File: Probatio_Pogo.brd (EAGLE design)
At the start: 21.5 x 8 mm, 5 parts

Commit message: Update Probatio_Pogo.brd
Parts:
- moved POGO1 2.00 mm to (4.00, 4.00)
- moved POGO2 2.00 mm to (7.00, 4.00)
- moved POGO3 2.00 mm to (10.0, 4.00)
- moved POGO4 2.00 mm to (13.0, 4.00)
- moved U$1 2.00 mm to (18.0, 4.00)
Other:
- board size 21.5 x 8 mm -> 23.5 x 8 mm
- board text added: "pogo-pcb v0.2.0"
- board text added: "probatio"
- board text removed: "Pogo-board v0.2.0"
- board text removed: "Probatio"
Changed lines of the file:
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@@
 <board>
 <plain>
-<wire x1="21.5" y1="1" x2="21.5" y2="7" width="0" layer="20"/>
+<wire x1="23.5" y1="1" x2="23.5" y2="7" width="0" layer="20"/>
 <wire x1="0" y1="7" x2="0" y2="1" width="0" layer="20"/>
-<wire x1="20.5" y1="8" x2="1" y2="8" width="0" layer="20"/>
-<text x="2.6" y="2.12" size="0.8128" layer="21" font="vector">1</text>
-<text x="5.4" y="2.09" size="0.8128" layer="21" font="vector">2</text>
-<text x="8.41" y="2.13" size="0.8128" layer="21" font="vector">3</text>
-<text x="11.51" y="2.14" size="0.8128" layer="21" font="vector">4</text>
-<text x="19.33" y="2.32" size="0.8128" layer="22" font="vector" rot="MR0">1</text>
-<text x="19.35" y="4.88" size="0.8128" layer="22" font="vector" rot="MR0">2</text>
-<text x="13.1" y="4.9" size="0.8128" layer="22" font="vector" rot="MR0">3</text>
-<text x="13.1" y="2.44" size="0.8128" layer="22" font="vector" rot="MR0">4</text>
-<wire x1="1" y1="0" x2="20.5" y2="0" width="0" layer="20"/>
+<wire x1="22.5" y1="8" x2="1" y2="8" width="0" layer="20"/>
+<text x="4.6" y="2.12" size="0.8128" layer="21" font="vector">1</text>
+<text x="7.4" y="2.09" size="0.8128" layer="21" font="vector">2</text>
+<text x="10.41" y="2.13" size="0.8128" layer="21" font="vector">3</text>
+<text x="13.51" y="2.14" size="0.8128" layer="21" font="vector">4</text>
+<text x="21.33" y="2.32" size="0.8128" layer="22" font="vector" rot="MR0">1</text>
+<text x="21.35" y="4.88" size="0.8128" layer="22" font="vector" rot="MR0">2</text>
+<text x="15.1" y="4.9" size="0.8128" layer="22" font="vector" rot="MR0">3</text>
+<text x="15.1" y="2.44" size="0.8128" layer="22" font="vector" rot="MR0">4</text>
+<wire x1="1" y1="0" x2="22.5" y2="0" width="0" layer="20"/>
 <wire x1="0" y1="7" x2="1" y2="8" width="0" layer="20" curve="-90"/>
 <wire x1="0" y1="1" x2="1" y2="0" width="0" layer="20" curve="90"/>
-<wire x1="20.5" y1="0" x2="21.5" y2="1" width="0" layer="20" curve="90"/>
-<wire x1="21.5" y1="7" x2="20.5" y2="8" width="0" layer="20" curve="90"/>
-<hole x="20.2" y="1.3" drill="2.2"/>
-<hole x="20.2" y="6.7" drill="2.2"/>
+<wire x1="22.5" y1="0" x2="23.5" y2="1" width="0" layer="20" curve="90"/>
+<wire x1="23.5" y1="7" x2="22.5" y2="8" width="0" layer="20" curve="90"/>
+<hole x="22.2" y="1.3" drill="2.2"/>
+<hole x="22.2" y="6.7" drill="2.2"/>
 <hole x="1.3" y="6.7" drill="2.2"/>
 <hole x="1.3" y="1.3" drill="2.2"/>
-<circle x="18.64" y="1.44" radius="0.183575" width="0.1524" layer="21"/>
-<circle x="2.97" y="4.96" radius="0.1627875" width="0.1524" layer="21"/>
-<text x="11.84" y="3.3" size="1.778" layer="22" font="vector" rot="MR0">Probatio</text>
-<text x="12" y="1" size="0.6096" layer="22" font="vector" rot="MR0">Pogo-board v0.2.0</text>
+<circle x="20.64" y="1.44" radius="0.183575" width="0.1524" layer="21"/>
+<circle x="4.97" y="4.96" radius="0.1627875" width="0.1524" layer="21"/>
+<text x="13.84" y="3.3" size="1.778" layer="22" font="vector" rot="MR0">probatio</text>
+<text x="14" y="1" size="0.6096" layer="22" font="vector" rot="MR0">pogo-pcb v0.2.0</text>
 </plain>
 <attributes>
@@
 </autorouter>
 <elements>
-<element name="POGO1" library="Batebit" package="POGO_PIN" value="POGO_PIN0900-0-15-20-76-14-11-0" x="2" y="4"/>
-<element name="POGO2" library="Batebit" package="POGO_PIN" value="POGO_PIN0900-0-15-20-76-14-11-0" x="5" y="4"/>
-<element name="POGO3" library="Batebit" package="POGO_PIN" value="POGO_PIN0900-0-15-20-76-14-11-0" x="8" y="4"/>
-<element name="POGO4" library="Batebit" package="POGO_PIN" value="POGO_PIN0900-0-15-20-76-14-11-0" x="11" y="4"/>
-<element name="U$1" library="Batebit" package="2X2" value="M02X22X2" x="16" y="4"/>
+<element name="POGO1" library="Batebit" package="POGO_PIN" value="POGO_PIN0900-0-15-20-76-14-11-0" x="4" y="4"/>
+<element name="POGO2" library="Batebit" package="POGO_PIN" value="POGO_PIN0900-0-15-20-76-14-11-0" x="7" y="4"/>
+<element name="POGO3" library="Batebit" package="POGO_PIN" value="POGO_PIN0900-0-15-20-76-14-11-0" x="10" y="4"/>
+<element name="POGO4" library="Batebit" package="POGO_PIN" value="POGO_PIN0900-0-15-20-76-14-11-0" x="13" y="4"/>
+<element name="U$1" library="Batebit" package="2X2" value="M02X22X2" x="18" y="4"/>
 </elements>
 <signals>
@@
 <contactref element="POGO4" pad="P$1"/>
 <contactref element="U$1" pad="1"/>
-<wire x1="11" y1="4" x2="12.25" y2="2.75" width="0.3556" layer="1"/>
-<wire x1="12.25" y1="2.75" x2="14.71" y2="2.75" width="0.3556" layer="1"/>
-<wire x1="14.71" y1="2.75" x2="14.73" y2="2.73" width="0.3048" layer="1"/>
+<wire x1="13" y1="4" x2="14.25" y2="2.75" width="0.3556" layer="1"/>
+<wire x1="14.25" y1="2.75" x2="16.71" y2="2.75" width="0.3556" layer="1"/>
+<wire x1="16.71" y1="2.75" x2="16.73" y2="2.73" width="0.3048" layer="1"/>
 </signal>
 <signal name="P1">
 <contactref element="POGO1" pad="P$1"/>
 <contactref element="U$1" pad="3"/>
-<wire x1="2" y1="4" x2="2" y2="3.35" width="0.3556" layer="1"/>
-<wire x1="2" y1="3.35" x2="4.11" y2="1.24" width="0.3556" layer="1"/>
-<wire x1="4.11" y1="1.24" x2="15.78" y2="1.24" width="0.3556" layer="1"/>
-<wire x1="15.78" y1="1.24" x2="17.27" y2="2.73" width="0.3556" layer="1"/>
+<wire x1="4" y1="4" x2="4" y2="3.35" width="0.3556" layer="1"/>
+<wire x1="4" y1="3.35" x2="6.11" y2="1.24" width="0.3556" layer="1"/>
+<wire x1="6.11" y1="1.24" x2="17.78" y2="1.24" width="0.3556" layer="1"/>
+<wire x1="17.78" y1="1.24" x2="19.27" y2="2.73" width="0.3556" layer="1"/>
 </signal>
 <signal name="P2">
 <contactref element="POGO2" pad="P$1"/>
 <contactref element="U$1" pad="4"/>
-<wire x1="5" y1="4" x2="5" y2="4.76" width="0.3556" layer="1"/>
-<wire x1="5" y1="4.76" x2="7.02" y2="6.78" width="0.3556" layer="1"/>
-<wire x1="7.02" y1="6.78" x2="15.76" y2="6.78" width="0.3556" layer="1"/>
-<wire x1="15.76" y1="6.78" x2="17.27" y2="5.27" width="0.3556" layer="1"/>
+<wire x1="7" y1="4" x2="7" y2="4.76" width="0.3556" layer="1"/>
+<wire x1="7" y1="4.76" x2="9.02" y2="6.78" width="0.3556" layer="1"/>
+<wire x1="9.02" y1="6.78" x2="17.76" y2="6.78" width="0.3556" layer="1"/>
+<wire x1="17.76" y1="6.78" x2="19.27" y2="5.27" width="0.3556" layer="1"/>
 </signal>
 <signal name="P3">
 <contactref element="POGO3" pad="P$1"/>
 <contactref element="U$1" pad="2"/>
-<wire x1="8" y1="4" x2="8.28" y2="4" width="0.3556" layer="1"/>
-<wire x1="8.28" y1="4" x2="9.95" y2="5.67" width="0.3556" layer="1"/>
-<wire x1="9.95" y1="5.67" x2="14.33" y2="5.67" width="0.3556" layer="1"/>
-<wire x1="14.33" y1="5.67" x2="14.73" y2="5.27" width="0.3556" layer="1"/>
+<wire x1="10" y1="4" x2="10.28" y2="4" width="0.3556" layer="1"/>
+<wire x1="10.28" y1="4" x2="11.95" y2="5.67" width="0.3556" layer="1"/>
+<wire x1="11.95" y1="5.67" x2="16.33" y2="5.67" width="0.3556" layer="1"/>
+<wire x1="16.33" y1="5.67" x2="16.73" y2="5.27" width="0.3556" layer="1"/>
 </signal>
 </signals>

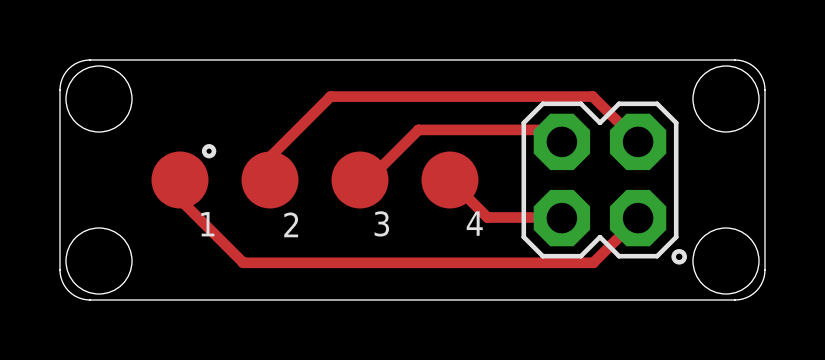
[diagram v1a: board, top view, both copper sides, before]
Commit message: Revert "Update Probatio_Pogo.brd"
This reverts commit b0f66f95d6e1f412cec8757038b3d4162e2bbc9a.
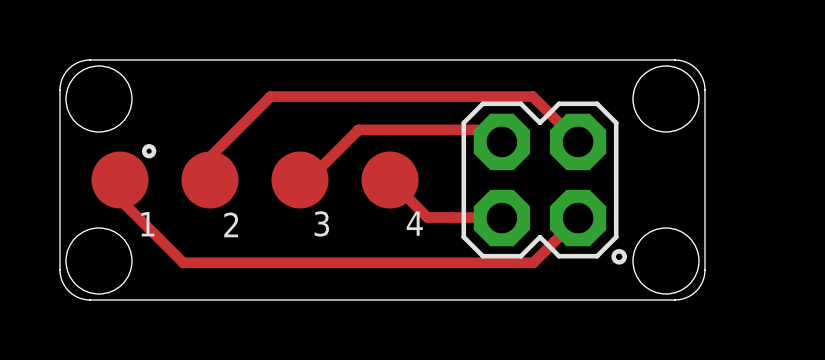
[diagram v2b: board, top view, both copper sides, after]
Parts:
- moved POGO1 2.00 mm to (2.00, 4.00)
- moved POGO2 2.00 mm to (5.00, 4.00)
- moved POGO3 2.00 mm to (8.00, 4.00)
- moved POGO4 2.00 mm to (11.0, 4.00)
- moved U$1 2.00 mm to (16.0, 4.00)
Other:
- board size 23.5 x 8 mm -> 21.5 x 8 mm
- board text added: "Pogo-board v0.2.0"
- board text added: "Probatio"
- board text removed: "pogo-pcb v0.2.0"
- board text removed: "probatio"
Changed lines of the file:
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@@
 <board>
 <plain>
-<wire x1="23.5" y1="1" x2="23.5" y2="7" width="0" layer="20"/>
+<wire x1="21.5" y1="1" x2="21.5" y2="7" width="0" layer="20"/>
 <wire x1="0" y1="7" x2="0" y2="1" width="0" layer="20"/>
-<wire x1="22.5" y1="8" x2="1" y2="8" width="0" layer="20"/>
-<text x="4.6" y="2.12" size="0.8128" layer="21" font="vector">1</text>
-<text x="7.4" y="2.09" size="0.8128" layer="21" font="vector">2</text>
-<text x="10.41" y="2.13" size="0.8128" layer="21" font="vector">3</text>
-<text x="13.51" y="2.14" size="0.8128" layer="21" font="vector">4</text>
-<text x="21.33" y="2.32" size="0.8128" layer="22" font="vector" rot="MR0">1</text>
-<text x="21.35" y="4.88" size="0.8128" layer="22" font="vector" rot="MR0">2</text>
-<text x="15.1" y="4.9" size="0.8128" layer="22" font="vector" rot="MR0">3</text>
-<text x="15.1" y="2.44" size="0.8128" layer="22" font="vector" rot="MR0">4</text>
-<wire x1="1" y1="0" x2="22.5" y2="0" width="0" layer="20"/>
+<wire x1="20.5" y1="8" x2="1" y2="8" width="0" layer="20"/>
+<text x="2.6" y="2.12" size="0.8128" layer="21" font="vector">1</text>
+<text x="5.4" y="2.09" size="0.8128" layer="21" font="vector">2</text>
+<text x="8.41" y="2.13" size="0.8128" layer="21" font="vector">3</text>
+<text x="11.51" y="2.14" size="0.8128" layer="21" font="vector">4</text>
+<text x="19.33" y="2.32" size="0.8128" layer="22" font="vector" rot="MR0">1</text>
+<text x="19.35" y="4.88" size="0.8128" layer="22" font="vector" rot="MR0">2</text>
+<text x="13.1" y="4.9" size="0.8128" layer="22" font="vector" rot="MR0">3</text>
+<text x="13.1" y="2.44" size="0.8128" layer="22" font="vector" rot="MR0">4</text>
+<wire x1="1" y1="0" x2="20.5" y2="0" width="0" layer="20"/>
 <wire x1="0" y1="7" x2="1" y2="8" width="0" layer="20" curve="-90"/>
 <wire x1="0" y1="1" x2="1" y2="0" width="0" layer="20" curve="90"/>
-<wire x1="22.5" y1="0" x2="23.5" y2="1" width="0" layer="20" curve="90"/>
-<wire x1="23.5" y1="7" x2="22.5" y2="8" width="0" layer="20" curve="90"/>
-<hole x="22.2" y="1.3" drill="2.2"/>
-<hole x="22.2" y="6.7" drill="2.2"/>
+<wire x1="20.5" y1="0" x2="21.5" y2="1" width="0" layer="20" curve="90"/>
+<wire x1="21.5" y1="7" x2="20.5" y2="8" width="0" layer="20" curve="90"/>
+<hole x="20.2" y="1.3" drill="2.2"/>
+<hole x="20.2" y="6.7" drill="2.2"/>
 <hole x="1.3" y="6.7" drill="2.2"/>
 <hole x="1.3" y="1.3" drill="2.2"/>
-<circle x="20.64" y="1.44" radius="0.183575" width="0.1524" layer="21"/>
-<circle x="4.97" y="4.96" radius="0.1627875" width="0.1524" layer="21"/>
-<text x="13.84" y="3.3" size="1.778" layer="22" font="vector" rot="MR0">probatio</text>
-<text x="14" y="1" size="0.6096" layer="22" font="vector" rot="MR0">pogo-pcb v0.2.0</text>
+<circle x="18.64" y="1.44" radius="0.183575" width="0.1524" layer="21"/>
+<circle x="2.97" y="4.96" radius="0.1627875" width="0.1524" layer="21"/>
+<text x="11.84" y="3.3" size="1.778" layer="22" font="vector" rot="MR0">Probatio</text>
+<text x="12" y="1" size="0.6096" layer="22" font="vector" rot="MR0">Pogo-board v0.2.0</text>
 </plain>
 <attributes>
@@
 </autorouter>
 <elements>
-<element name="POGO1" library="Batebit" package="POGO_PIN" value="POGO_PIN0900-0-15-20-76-14-11-0" x="4" y="4"/>
-<element name="POGO2" library="Batebit" package="POGO_PIN" value="POGO_PIN0900-0-15-20-76-14-11-0" x="7" y="4"/>
-<element name="POGO3" library="Batebit" package="POGO_PIN" value="POGO_PIN0900-0-15-20-76-14-11-0" x="10" y="4"/>
-<element name="POGO4" library="Batebit" package="POGO_PIN" value="POGO_PIN0900-0-15-20-76-14-11-0" x="13" y="4"/>
-<element name="U$1" library="Batebit" package="2X2" value="M02X22X2" x="18" y="4"/>
+<element name="POGO1" library="Batebit" package="POGO_PIN" value="POGO_PIN0900-0-15-20-76-14-11-0" x="2" y="4"/>
+<element name="POGO2" library="Batebit" package="POGO_PIN" value="POGO_PIN0900-0-15-20-76-14-11-0" x="5" y="4"/>
+<element name="POGO3" library="Batebit" package="POGO_PIN" value="POGO_PIN0900-0-15-20-76-14-11-0" x="8" y="4"/>
+<element name="POGO4" library="Batebit" package="POGO_PIN" value="POGO_PIN0900-0-15-20-76-14-11-0" x="11" y="4"/>
+<element name="U$1" library="Batebit" package="2X2" value="M02X22X2" x="16" y="4"/>
 </elements>
 <signals>
@@
 <contactref element="POGO4" pad="P$1"/>
 <contactref element="U$1" pad="1"/>
-<wire x1="13" y1="4" x2="14.25" y2="2.75" width="0.3556" layer="1"/>
-<wire x1="14.25" y1="2.75" x2="16.71" y2="2.75" width="0.3556" layer="1"/>
-<wire x1="16.71" y1="2.75" x2="16.73" y2="2.73" width="0.3048" layer="1"/>
+<wire x1="11" y1="4" x2="12.25" y2="2.75" width="0.3556" layer="1"/>
+<wire x1="12.25" y1="2.75" x2="14.71" y2="2.75" width="0.3556" layer="1"/>
+<wire x1="14.71" y1="2.75" x2="14.73" y2="2.73" width="0.3048" layer="1"/>
 </signal>
 <signal name="P1">
 <contactref element="POGO1" pad="P$1"/>
 <contactref element="U$1" pad="3"/>
-<wire x1="4" y1="4" x2="4" y2="3.35" width="0.3556" layer="1"/>
-<wire x1="4" y1="3.35" x2="6.11" y2="1.24" width="0.3556" layer="1"/>
-<wire x1="6.11" y1="1.24" x2="17.78" y2="1.24" width="0.3556" layer="1"/>
-<wire x1="17.78" y1="1.24" x2="19.27" y2="2.73" width="0.3556" layer="1"/>
+<wire x1="2" y1="4" x2="2" y2="3.35" width="0.3556" layer="1"/>
+<wire x1="2" y1="3.35" x2="4.11" y2="1.24" width="0.3556" layer="1"/>
+<wire x1="4.11" y1="1.24" x2="15.78" y2="1.24" width="0.3556" layer="1"/>
+<wire x1="15.78" y1="1.24" x2="17.27" y2="2.73" width="0.3556" layer="1"/>
 </signal>
 <signal name="P2">
 <contactref element="POGO2" pad="P$1"/>
 <contactref element="U$1" pad="4"/>
-<wire x1="7" y1="4" x2="7" y2="4.76" width="0.3556" layer="1"/>
-<wire x1="7" y1="4.76" x2="9.02" y2="6.78" width="0.3556" layer="1"/>
-<wire x1="9.02" y1="6.78" x2="17.76" y2="6.78" width="0.3556" layer="1"/>
-<wire x1="17.76" y1="6.78" x2="19.27" y2="5.27" width="0.3556" layer="1"/>
+<wire x1="5" y1="4" x2="5" y2="4.76" width="0.3556" layer="1"/>
+<wire x1="5" y1="4.76" x2="7.02" y2="6.78" width="0.3556" layer="1"/>
+<wire x1="7.02" y1="6.78" x2="15.76" y2="6.78" width="0.3556" layer="1"/>
+<wire x1="15.76" y1="6.78" x2="17.27" y2="5.27" width="0.3556" layer="1"/>
 </signal>
 <signal name="P3">
 <contactref element="POGO3" pad="P$1"/>
 <contactref element="U$1" pad="2"/>
-<wire x1="10" y1="4" x2="10.28" y2="4" width="0.3556" layer="1"/>
-<wire x1="10.28" y1="4" x2="11.95" y2="5.67" width="0.3556" layer="1"/>
-<wire x1="11.95" y1="5.67" x2="16.33" y2="5.67" width="0.3556" layer="1"/>
-<wire x1="16.33" y1="5.67" x2="16.73" y2="5.27" width="0.3556" layer="1"/>
+<wire x1="8" y1="4" x2="8.28" y2="4" width="0.3556" layer="1"/>
+<wire x1="8.28" y1="4" x2="9.95" y2="5.67" width="0.3556" layer="1"/>
+<wire x1="9.95" y1="5.67" x2="14.33" y2="5.67" width="0.3556" layer="1"/>
+<wire x1="14.33" y1="5.67" x2="14.73" y2="5.27" width="0.3556" layer="1"/>
 </signal>
 </signals>
